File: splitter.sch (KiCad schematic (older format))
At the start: 5 parts

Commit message: Schematic finished
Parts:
- gave numbers to parts that had none: 5
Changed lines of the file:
@@
 LIBS:2450bl15b050
 LIBS:tlv4172
+LIBS:l4940d2t12-tr
+LIBS:tps54308
+LIBS:l78l33abu
+LIBS:adp150aujz-18
 LIBS:radar-cache
+LIBS:hn1c01fu
 EELAYER 25 0
 EELAYER END
 $Descr A4 11693 8268
 encoding utf-8
-Sheet 3 7
+Sheet 3 8
 Title ""
 Date ""
@@
 $EndDescr
 $Comp
-L PD2425N5050S2 U?
+L PD2425N5050S2 U301
 U 1 1 59D54F30
 P 5430 3800
-F 0 "U?" H 5430 3850 60  0000 C CNN
+F 0 "U301" H 5430 3850 60  0000 C CNN
 F 1 "PD2425N5050S2" H 6030 3500 60  0000 C CNN
 F 2 "" H 5430 3800 60  0001 C CNN
@@
 $EndComp
 $Comp
-L taper T?
+L taper T301
 U 1 1 59D55000
 P 5430 2780
-F 0 "T?" H 5430 2930 60  0000 C CNN
+F 0 "T301" H 5430 2930 60  0000 C CNN
 F 1 "taper" H 5330 2630 60  0000 C CNN
 F 2 "" H 5430 2780 60  0001 C CNN
@@
 $EndComp
 $Comp
-L taper T?
+L taper T302
 U 1 1 59D5510D
 P 4300 3900
-F 0 "T?" H 4300 4050 60  0000 C CNN
+F 0 "T302" H 4300 4050 60  0000 C CNN
 F 1 "taper" H 4200 3750 60  0000 C CNN
 F 2 "" H 4300 3900 60  0001 C CNN
@@
 $EndComp
 $Comp
-L taper T?
+L taper T303
 U 1 1 59D5516E
 P 6620 3900
-F 0 "T?" H 6620 4050 60  0000 C CNN
+F 0 "T303" H 6620 4050 60  0000 C CNN
 F 1 "taper" H 6520 3750 60  0000 C CNN
 F 2 "" H 6620 3900 60  0001 C CNN
@@
 OUT2
 $Comp
-L GND #PWR?
+L GND #PWR030
 U 1 1 59D551D4
 P 5430 4380
-F 0 "#PWR?" H 5430 4130 50  0001 C CNN
+F 0 "#PWR030" H 5430 4130 50  0001 C CNN
 F 1 "GND" H 5430 4230 50  0000 C CNN
 F 2 "" H 5430 4380 50  0001 C CNN
@@
 	6920 3900 7070 3900
 $Comp
-L R_Small R?
+L R_Small R301
 U 1 1 59D554E5
 P 5090 4300
-F 0 "R?" H 5120 4320 50  0000 L CNN
+F 0 "R301" H 5120 4320 50  0000 L CNN
 F 1 "100" H 5120 4260 50  0000 L CNN
 F 2 "" H 5090 4300 50  0001 C CNN

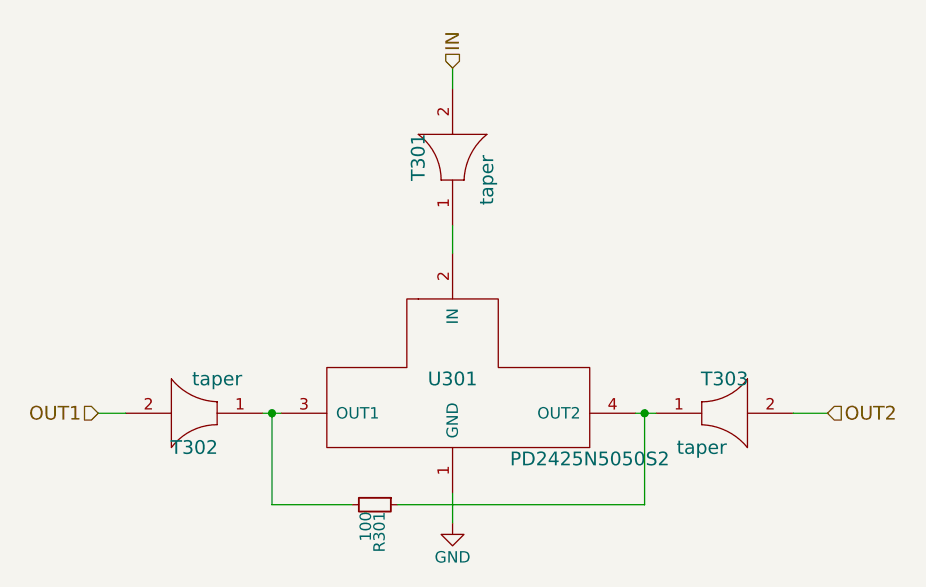
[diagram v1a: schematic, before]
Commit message: Assign a lot of footprints, fix l78l33abu part (input and output were reversed)
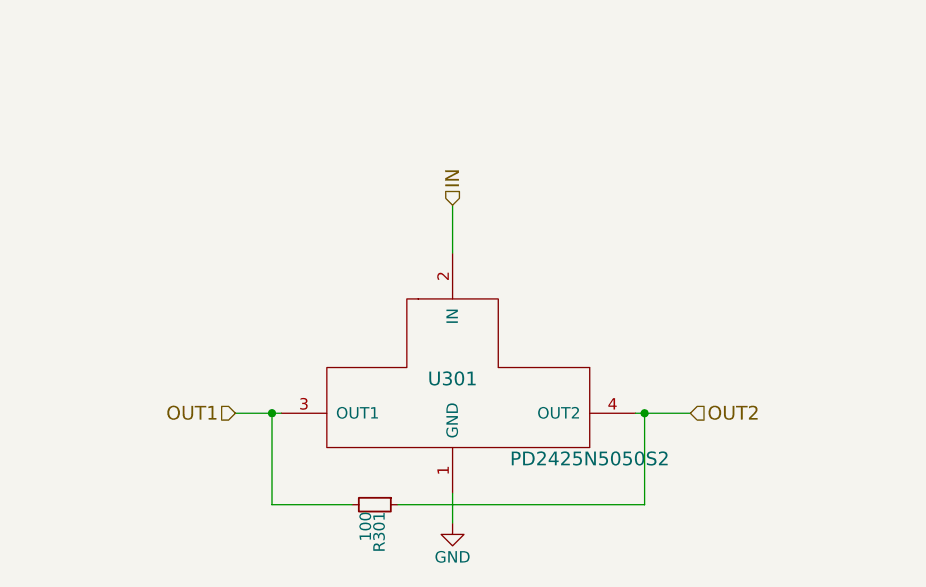
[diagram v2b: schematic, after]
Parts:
- removed T301, T302, T303: taper, symbol taper
- R301: footprint (none) -> Resistors_SMD:R_0603_HandSoldering
- U301: footprint (none) -> rajsradar:PD2425N5050S2
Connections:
- net IN: now also U301.2 (IN)
- net OUT1: now also R301.2, U301.3 (OUT1)
- net OUT2: now also R301.1, U301.4 (OUT2)
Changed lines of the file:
@@
 F 0 "U301" H 5430 3850 60  0000 C CNN
 F 1 "PD2425N5050S2" H 6030 3500 60  0000 C CNN
-F 2 "" H 5430 3800 60  0001 C CNN
+F 2 "rajsradar:PD2425N5050S2" H 5430 3800 60  0001 C CNN
 F 3 "" H 5430 3800 60  0001 C CNN
 	1    5430 3800
 	1    0    0    -1
 $EndComp
-$Comp
-L taper T301
-U 1 1 59D55000
-P 5430 2780
-F 0 "T301" H 5430 2930 60  0000 C CNN
-F 1 "taper" H 5330 2630 60  0000 C CNN
-F 2 "" H 5430 2780 60  0001 C CNN
-F 3 "" H 5430 2780 60  0001 C CNN
-	1    5430 2780
-	0    -1   -1   0
-$EndComp
-$Comp
-L taper T302
-U 1 1 59D5510D
-P 4300 3900
-F 0 "T302" H 4300 4050 60  0000 C CNN
-F 1 "taper" H 4200 3750 60  0000 C CNN
-F 2 "" H 4300 3900 60  0001 C CNN
-F 3 "" H 4300 3900 60  0001 C CNN
-	1    4300 3900
-	-1   0    0    1
-$EndComp
-$Comp
-L taper T303
-U 1 1 59D5516E
-P 6620 3900
-F 0 "T303" H 6620 4050 60  0000 C CNN
-F 1 "taper" H 6520 3750 60  0000 C CNN
-F 2 "" H 6620 3900 60  0001 C CNN
-F 3 "" H 6620 3900 60  0001 C CNN
-	1    6620 3900
-	1    0    0    -1
-$EndComp
-Text HLabel 5430 2390 1    60   Input ~ 0
+Text HLabel 5430 2990 1    60   Input ~ 0
 IN
-Text HLabel 3880 3900 0    60   Input ~ 0
+Text HLabel 4480 3900 0    60   Input ~ 0
 OUT1
-Text HLabel 7070 3900 2    60   Input ~ 0
+Text HLabel 6470 3900 2    60   Input ~ 0
 OUT2
 $Comp
-L GND #PWR030
+L GND #PWR031
 U 1 1 59D551D4
 P 5430 4380
-F 0 "#PWR030" H 5430 4130 50  0001 C CNN
+F 0 "#PWR031" H 5430 4130 50  0001 C CNN
 F 1 "GND" H 5430 4230 50  0000 C CNN
 F 2 "" H 5430 4380 50  0001 C CNN
@@
 	5430 4380 5430 4250
 Wire Wire Line
-	4600 3900 4680 3900
+	4480 3900 4680 3900
 Wire Wire Line
-	4000 3900 3880 3900
+	5430 2990 5430 3200
 Wire Wire Line
-	5430 3080 5430 3200
-Wire Wire Line
-	5430 2390 5430 2480
-Wire Wire Line
-	6230 3900 6320 3900
-Wire Wire Line
-	6920 3900 7070 3900
+	6230 3900 6470 3900
 $Comp
 L R_Small R301
@@
 F 0 "R301" H 5120 4320 50  0000 L CNN
 F 1 "100" H 5120 4260 50  0000 L CNN
-F 2 "" H 5090 4300 50  0001 C CNN
+F 2 "Resistors_SMD:R_0603_HandSoldering" H 5090 4300 50  0001 C CNN
 F 3 "" H 5090 4300 50  0001 C CNN
 	1    5090 4300
